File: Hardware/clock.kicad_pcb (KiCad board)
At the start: 2 copper layers, 98 x 55 mm, 53 parts, among them J1 Conn_02x05_Counter_Clockwise, J2 Conn_01x02_Male, J3 USB_B_Micro, J4 Barrel_Jack, Q1 2N7002ET1G, SW1 SW_Push, SW2 SW_Push, SW3 SW_Push, U1 STM32F103C8Tx, U2 UA78M33CDCY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

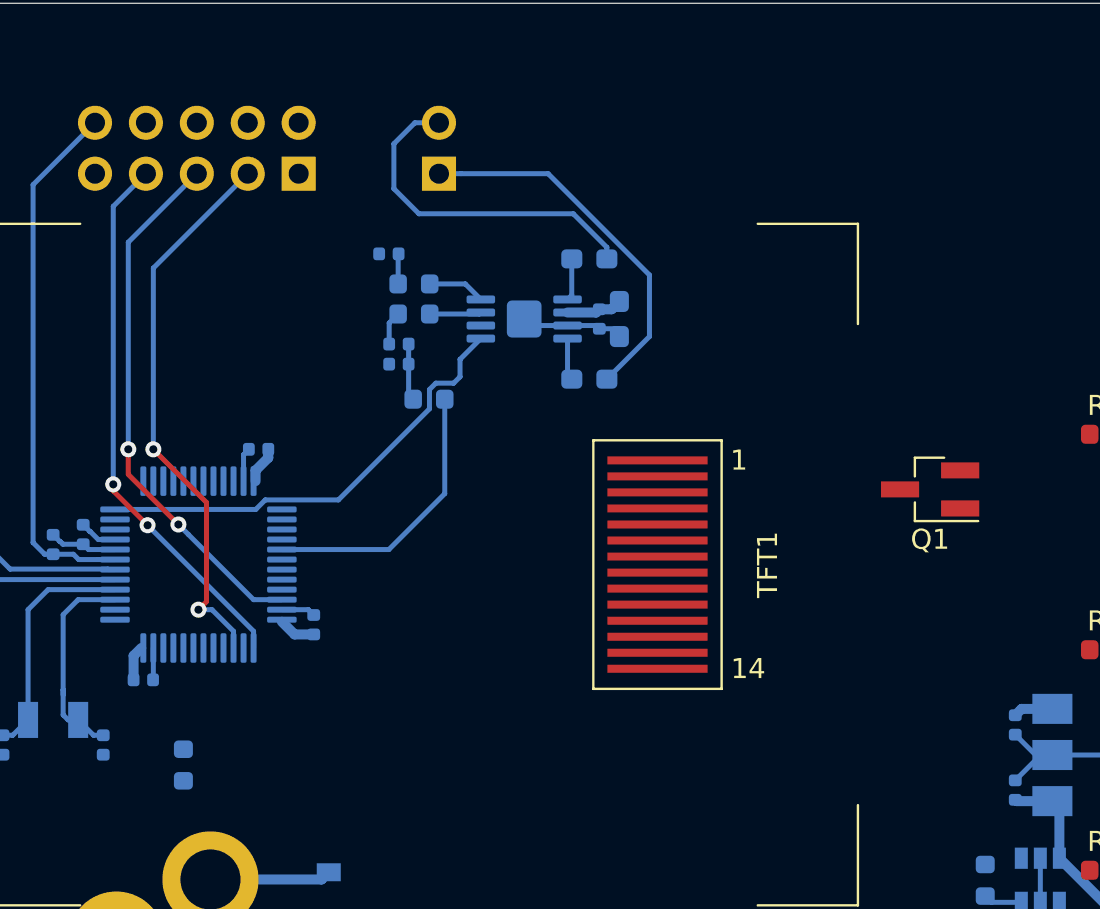
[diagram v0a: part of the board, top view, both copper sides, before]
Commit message: Added filter for amplifier supply. Some routing.
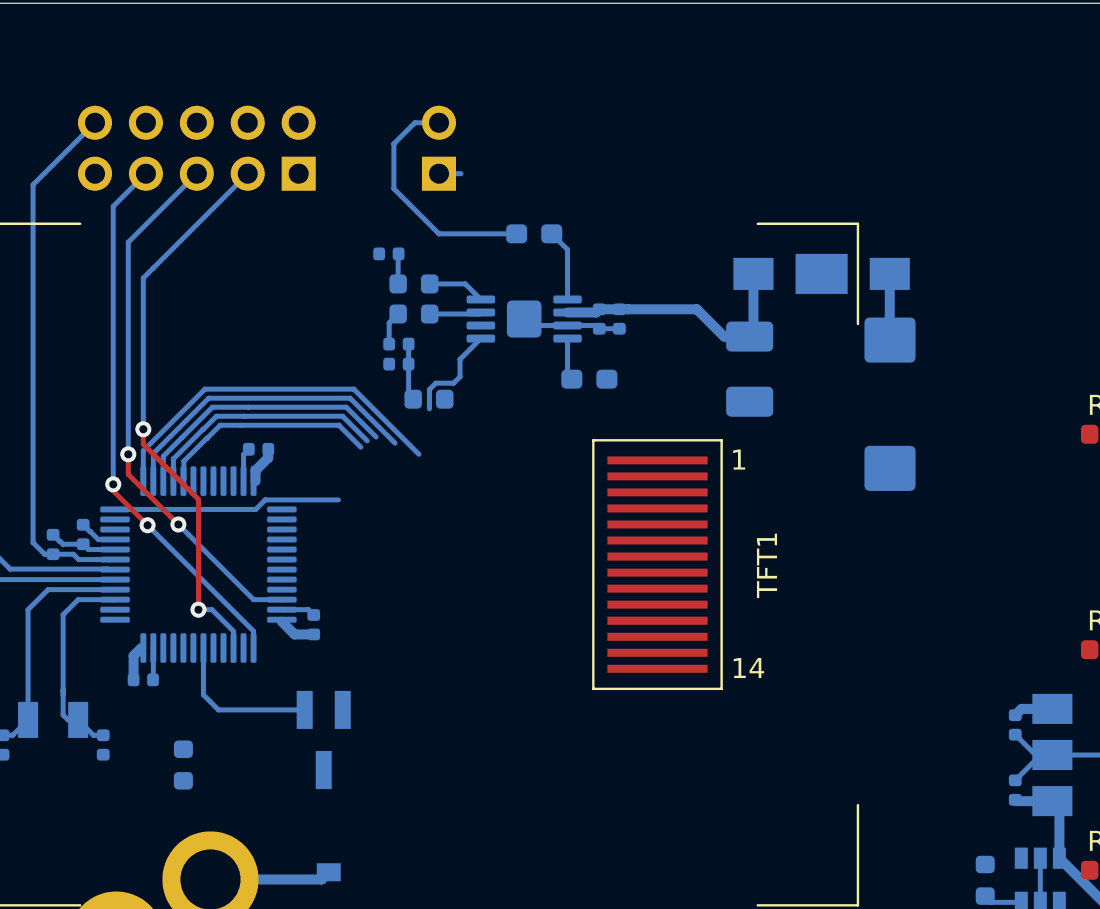
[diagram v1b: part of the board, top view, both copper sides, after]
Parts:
- added C20: 220U, Capacitor_Tantalum_SMD:CP_EIA-7343-20_Kemet-V_Pad2.25x2.55mm_HandSolder, B.Cu at (154.7, 85.7)
- added C21: 33U, Capacitor_Tantalum_SMD:CP_EIA-3528-21_Kemet-B_Pad1.50x2.35mm_HandSolder, B.Cu at (147.7, 83.9)
- added FL1: NFE61PT472C1H9L, Footprints:6816, B.Cu at (151.3, 79.2)
- C17: footprint Capacitor_SMD:C_0603_1608Metric_Pad1.05x0.95mm_HandSolder -> Capacitor_SMD:C_0402_1005Metric
- Q1: moved to B.Cu
- moved Q1 32.7 mm to (126.5, 102.4), turned to 270 degrees
- moved FB2 3.02 mm to (137.0, 77.2), turned to 0 degrees
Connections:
- C17 pad 2: +3V3 -> +3.3VA
- C18 pad 2: +3V3 -> +3.3VA
- U3 pad 6: +3V3 -> +3.3VA
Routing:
- net /TFT_RS: track 0.00 -> 17.9 mm
- net Net-(FB1-Pad1): track 18.7 -> 1.10 mm
- net /TFT_CS: track 0.00 -> 15.5 mm
- net /AUDIO: track 14.0 -> 0.00 mm
- net /TFT_SCLK: track 0.00 -> 13.5 mm
- net +3.3VA: track 0.00 -> 12.9 mm
- net /TFT_DC: track 0.00 -> 12.2 mm
- net /TFT_MOSI: track 0.00 -> 11.0 mm
- net /TFT_BL: track 0.00 -> 7.70 mm
- net /AMP_ON: track 22.9 -> 16.4 mm
- net Net-(FB2-Pad1): track 17.3 -> 12.0 mm
- net /AUDIO_OUT_+: track 2.11 -> 3.60 mm

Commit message: Routing complete
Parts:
- added R11: 100R, Resistor_SMD:R_0603_1608Metric, B.Cu at (122.2, 100.7)
- C15, C16, C19: moved to F.Cu
- J4: footprint Foodprints:PJ-102A -> Footprints:DC-005-SMT
- moved C19 126.8 mm to (155.0, 90.9), turned to 180 degrees
- moved C16 106.2 mm to (155.0, 95.7), turned to 180 degrees
- moved C15 87.1 mm to (155.0, 96.7), turned to 180 degrees
- moved D3 13.8 mm to (113.0, 109.9), turned to 270 degrees
- moved J4 11.3 mm to (122.0, 107.4), turned to 270 degrees
- moved R8 6.19 mm to (126.2, 82.5), turned to 180 degrees
- moved C12 2.56 mm to (128.2, 82.0), turned to 270 degrees
- moved R7 1.21 mm to (166.5, 87.8), turned to 90 degrees
- moved R5 1.14 mm to (166.5, 98.3), turned to 90 degrees
- moved R6 1.14 mm to (166.5, 109.3), turned to 90 degrees
- moved C5 0.56 mm to (113.9, 92.2)
- moved C13 0.51 mm to (129.7, 82.5), turned to 180 degrees
- moved C1 0.50 mm to (126.0, 96.2)
- moved C8 0.50 mm to (112.5, 92.7)
- moved TFT1 0.10 mm to (130.1, 93.7)
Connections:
- Q1 pad 1: /TFT_BL -> Net-(Q1-Pad1)
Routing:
- net +3V3: track 42.7 -> 252.4 mm, vias 0 -> 8
- net +5V: track 9.54 -> 170.7 mm
- net /BTN_DN: track 10.6 -> 101.1 mm, vias 0 -> 1
- net /BTN_UP: track 10.6 -> 93.6 mm, vias 0 -> 1
- net /SWDIO: track 26.4 -> 87.3 mm, vias 2 -> 0
- net /3VB: track 0.00 -> 56.2 mm, vias 0 -> 2
- net /SWCLK: track 27.2 -> 78.1 mm, vias 2 -> 0
- net /BTN_SEL: track 10.5 -> 60.9 mm, vias 0 -> 3
- net /SWO: track 28.1 -> 77.8 mm, vias 2 -> 0
- net /USB_DM: track 5.17 -> 47.8 mm
- net /USB_DP: track 3.87 -> 45.3 mm
- net Net-(FB1-Pad1): track 1.10 -> 34.6 mm
- net GND: track 39.2 -> 71.0 mm, vias 0 -> 32
- net /LED-: track 0.00 -> 24.4 mm, vias 0 -> 3
- net /AUDIO: track 0.00 -> 22.5 mm
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- added copper zone on B.Cu, net GND
- added copper zone on F.Cu, net GND
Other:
- board text added: "3V3"
- board text added: "CLK"
- board text added: "GND"
- board text added: "RST"
- board text added: "SPEAKER"
- board text added: "SWD"
- board text added: "SWO"
- board text removed: "Barrel jack PTH over TFT area, may need to move"

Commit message: DC jack was round the wrong way. Added proper step model for it. Added Freecad model.
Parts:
- moved J4 15.4 mm to (122.1, 122.8), turned to 90 degrees
- moved J2 8.00 mm to (140.2, 74.2)
- moved J1 7.03 mm to (132.2, 73.5)
- moved FB2 1.93 mm to (138.6, 78.2), turned to 270 degrees
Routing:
- net Net-(D3-Pad2): track 9.54 -> 24.3 mm
- net /RESET: track 44.8 -> 58.6 mm
- net Net-(FB1-Pad1): track 34.6 -> 26.6 mm
- net /SWCLK: track 78.1 -> 86.0 mm
- net /SWDIO: track 87.3 -> 94.4 mm
- net /SWO: track 77.8 -> 84.8 mm
- net Net-(FB2-Pad1): track 9.97 -> 6.36 mm
- net +3V3: track 252.4 -> 249.8 mm, vias 8 -> 9
- net /AUDIO_OUT_+: track 3.60 -> 1.39 mm
- net +5V: track 170.7 -> 168.8 mm
- net /BTN_UP: track 93.6 -> 92.3 mm
- net /BTN_DN: track 101.1 -> 99.8 mm
- net GND: vias 32 -> 31
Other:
- board text removed: "3V3"
- board text removed: "CLK"
- board text removed: "GND"
- board text removed: "RST"
- board text removed: "SWD"
- board text removed: "SWO"

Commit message: Added FreeCAD model of enclosure + PCB. Small changes to PCB layout. Added STEP model of TFT display.
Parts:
- U3: footprint Package_SO:MSOP-8-1EP_3x3mm_P0.65mm_EP1.73x1.85mm -> Package_SO:MSOP-8-1EP_3x3mm_P0.65mm_EP1.73x1.85mm_ThermalVias
- moved FB2 0.23 mm to (138.6, 78.0)
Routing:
- net GND: track 71.0 -> 74.7 mm, vias 31 -> 32
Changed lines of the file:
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@@
     (thickness 1.6)
     (drawings 8797)
-    (tracks 577)
+    (tracks 580)
     (zones 0)
     (modules 57)
@@
   (page A4)
   (layers
-    (0 F.Cu signal)
+    (0 F.Cu signal hide)
     (31 B.Cu signal)
     (34 B.Paste user hide)
@@
     (44 Edge.Cuts user)
     (45 Margin user)
-    (46 B.CrtYd user hide)
-    (47 F.CrtYd user)
+    (46 B.CrtYd user)
+    (47 F.CrtYd user hide)
   )
   (setup
-    (last_trace_width 1)
+    (last_trace_width 0.25)
     (user_trace_width 0.24)
     (user_trace_width 0.5)
@@
     (uvia_drill 0.1)
   )
+  (module Package_SO:MSOP-8-1EP_3x3mm_P0.65mm_EP1.73x1.85mm_ThermalVias (layer B.Cu)
+    (at 136.4639 81.4)
+    (descr "MSOP, 8 Pin (http://www.ti.com/lit/ds/symlink/lm25085.pdf#page=32), generated with kicad-footprint-generator ipc_gullwing_generator.py")
+    (tags "MSOP SO")
+    (attr smd)
+    (fp_text reference U3 (at 0 2.45) (layer B.SilkS)
+      (effects (font (size 1 1) (thickness 0.15)) (justify mirror))
+    )
+    (fp_text value TPA2005D1DRB (at 0 -2.45) (layer B.Fab)
+      (effects (font (size 1 1) (thickness 0.15)) (justify mirror))
+    )
+    (fp_text user %R (at 0 0) (layer B.Fab)
+      (effects (font (size 0.75 0.75) (thickness 0.11)) (justify mirror))
+    )
+    (fp_line (start 3.12 1.75) (end -3.12 1.75) (layer B.CrtYd) (width 0.05))
+    (fp_line (start 3.12 -1.75) (end 3.12 1.75) (layer B.CrtYd) (width 0.05))
+    (fp_line (start -3.12 -1.75) (end 3.12 -1.75) (layer B.CrtYd) (width 0.05))
+    (fp_line (start -3.12 1.75) (end -3.12 -1.75) (layer B.CrtYd) (width 0.05))
+    (fp_line (start -1.5 0.75) (end -0.75 1.5) (layer B.Fab) (width 0.1))
+    (fp_line (start -1.5 -1.5) (end -1.5 0.75) (layer B.Fab) (width 0.1))
+    (fp_line (start 1.5 -1.5) (end -1.5 -1.5) (layer B.Fab) (width 0.1))
+    (fp_line (start 1.5 1.5) (end 1.5 -1.5) (layer B.Fab) (width 0.1))
+    (fp_line (start -0.75 1.5) (end 1.5 1.5) (layer B.Fab) (width 0.1))
+    (fp_line (start 0 1.61) (end -2.875 1.61) (layer B.SilkS) (width 0.12))
+    (fp_line (start 0 1.61) (end 1.5 1.61) (layer B.SilkS) (width 0.12))
+    (fp_line (start 0 -1.61) (end -1.5 -1.61) (layer B.SilkS) (width 0.12))
+    (fp_line (start 0 -1.61) (end 1.5 -1.61) (layer B.SilkS) (width 0.12))
+    (pad 8 smd roundrect (at 2.1625 0.975) (size 1.425 0.4) (layers B.Cu B.Paste B.Mask) (roundrect_rratio 0.25)
+      (net 19 /AUDIO_OUT_-))
+    (pad 7 smd roundrect (at 2.1625 0.325) (size 1.425 0.4) (layers B.Cu B.Paste B.Mask) (roundrect_rratio 0.25)
+      (net 2 GND))
+    (pad 6 smd roundrect (at 2.1625 -0.325) (size 1.425 0.4) (layers B.Cu B.Paste B.Mask) (roundrect_rratio 0.25)
+      (net 65 +3.3VA))
+    (pad 5 smd roundrect (at 2.1625 -0.975) (size 1.425 0.4) (layers B.Cu B.Paste B.Mask) (roundrect_rratio 0.25)
+      (net 20 /AUDIO_OUT_+))
+    (pad 4 smd roundrect (at -2.1625 -0.975) (size 1.425 0.4) (layers B.Cu B.Paste B.Mask) (roundrect_rratio 0.25)
+      (net 39 "Net-(R10-Pad1)"))
+    (pad 3 smd roundrect (at -2.1625 -0.325) (size 1.425 0.4) (layers B.Cu B.Paste B.Mask) (roundrect_rratio 0.25)
+      (net 38 "Net-(R9-Pad1)"))
+    (pad 2 smd roundrect (at -2.1625 0.325) (size 1.425 0.4) (layers B.Cu B.Paste B.Mask) (roundrect_rratio 0.25))
+    (pad 1 smd roundrect (at -2.1625 0.975) (size 1.425 0.4) (layers B.Cu B.Paste B.Mask) (roundrect_rratio 0.25)
+      (net 48 /AMP_ON))
+    (pad "" smd roundrect (at 0.43 -0.46) (size 0.72 0.77) (layers B.Paste) (roundrect_rratio 0.25))
+    (pad "" smd roundrect (at 0.43 0.46) (size 0.72 0.77) (layers B.Paste) (roundrect_rratio 0.25))
+    (pad "" smd roundrect (at -0.43 -0.46) (size 0.72 0.77) (layers B.Paste) (roundrect_rratio 0.25))
+    (pad "" smd roundrect (at -0.43 0.46) (size 0.72 0.77) (layers B.Paste) (roundrect_rratio 0.25))
+    (pad 9 smd roundrect (at 0 0) (size 1.6 1.8) (layers F.Cu) (roundrect_rratio 0.15625)
+      (net 2 GND))
+    (pad 9 thru_hole circle (at 0.55 -0.65) (size 0.5 0.5) (drill 0.2) (layers *.Cu)
+      (net 2 GND))
+    (pad 9 thru_hole circle (at -0.55 -0.65) (size 0.5 0.5) (drill 0.2) (layers *.Cu)
+      (net 2 GND))
+    (pad 9 thru_hole circle (at 0.55 0.65) (size 0.5 0.5) (drill 0.2) (layers *.Cu)
+      (net 2 GND))
+    (pad 9 thru_hole circle (at -0.55 0.65) (size 0.5 0.5) (drill 0.2) (layers *.Cu)
+      (net 2 GND))
+    (pad 9 smd roundrect (at 0 0) (size 1.73 1.85) (layers B.Cu B.Mask) (roundrect_rratio 0.144509)
+      (net 2 GND))
+    (model ${KISYS3DMOD}/Package_SO.3dshapes/MSOP-8-1EP_3x3mm_P0.65mm_EP1.73x1.85mm.wrl
+      (at (xyz 0 0 0))
+      (scale (xyz 1 1 1))
+      (rotate (xyz 0 0 0))
+    )
+  )
   (module Footprints:DC-005-SMT (layer B.Cu)
     (at 122.1479 122.8165 90)
@@
   )
   (module Resistor_SMD:R_0603_1608Metric_Pad1.05x0.95mm_HandSolder (layer B.Cu)
-    (at 138.5944 78.176 270)
+    (at 138.5944 77.95 270)
     (descr "Resistor SMD 0603 (1608 Metric), square (rectangular) end terminal, IPC_7351 nominal with elongated pad for handsoldering. (Body size source: http://www.tortai-tech.com/upload/download/2011102023233369053.pdf), generated with kicad-footprint-generator")
     (tags "resistor handsolder")
@@
     )
   )
-  (module Package_SO:MSOP-8-1EP_3x3mm_P0.65mm_EP1.73x1.85mm (layer B.Cu)
-    (at 136.4639 81.4)
-    (descr "MSOP, 8 Pin (http://www.ti.com/lit/ds/symlink/lm25085.pdf#page=32), generated with kicad-footprint-generator ipc_gullwing_generator.py")
-    (tags "MSOP SO")
-    (attr smd)
-    (fp_text reference U3 (at 0 2.45) (layer B.SilkS)
-      (effects (font (size 1 1) (thickness 0.15)) (justify mirror))
-    )
-    (fp_text value TPA2005D1DRB (at 0 -2.45) (layer B.Fab)
-      (effects (font (size 1 1) (thickness 0.15)) (justify mirror))
-    )
-    (fp_line (start 0 -1.61) (end 1.5 -1.61) (layer B.SilkS) (width 0.12))
-    (fp_line (start 0 -1.61) (end -1.5 -1.61) (layer B.SilkS) (width 0.12))
-    (fp_line (start 0 1.61) (end 1.5 1.61) (layer B.SilkS) (width 0.12))
-    (fp_line (start 0 1.61) (end -2.875 1.61) (layer B.SilkS) (width 0.12))
-    (fp_line (start -0.75 1.5) (end 1.5 1.5) (layer B.Fab) (width 0.1))
-    (fp_line (start 1.5 1.5) (end 1.5 -1.5) (layer B.Fab) (width 0.1))
-    (fp_line (start 1.5 -1.5) (end -1.5 -1.5) (layer B.Fab) (width 0.1))
-    (fp_line (start -1.5 -1.5) (end -1.5 0.75) (layer B.Fab) (width 0.1))
-    (fp_line (start -1.5 0.75) (end -0.75 1.5) (layer B.Fab) (width 0.1))
-    (fp_line (start -3.12 1.75) (end -3.12 -1.75) (layer B.CrtYd) (width 0.05))
-    (fp_line (start -3.12 -1.75) (end 3.12 -1.75) (layer B.CrtYd) (width 0.05))
-    (fp_line (start 3.12 -1.75) (end 3.12 1.75) (layer B.CrtYd) (width 0.05))
-    (fp_line (start 3.12 1.75) (end -3.12 1.75) (layer B.CrtYd) (width 0.05))
-    (fp_text user %R (at 0 0) (layer B.Fab)
-      (effects (font (size 0.75 0.75) (thickness 0.11)) (justify mirror))
-    )
-    (pad 9 smd roundrect (at 0 0) (size 1.73 1.85) (layers B.Cu B.Mask) (roundrect_rratio 0.144509)
-      (net 2 GND))
-    (pad "" smd roundrect (at -0.43 0.46) (size 0.7 0.75) (layers B.Paste) (roundrect_rratio 0.25))
-    (pad "" smd roundrect (at -0.43 -0.46) (size 0.7 0.75) (layers B.Paste) (roundrect_rratio 0.25))
-    (pad "" smd roundrect (at 0.43 0.46) (size 0.7 0.75) (layers B.Paste) (roundrect_rratio 0.25))
-    (pad "" smd roundrect (at 0.43 -0.46) (size 0.7 0.75) (layers B.Paste) (roundrect_rratio 0.25))
-    (pad 1 smd roundrect (at -2.1625 0.975) (size 1.425 0.4) (layers B.Cu B.Paste B.Mask) (roundrect_rratio 0.25)
-      (net 48 /AMP_ON))
-    (pad 2 smd roundrect (at -2.1625 0.325) (size 1.425 0.4) (layers B.Cu B.Paste B.Mask) (roundrect_rratio 0.25))
-    (pad 3 smd roundrect (at -2.1625 -0.325) (size 1.425 0.4) (layers B.Cu B.Paste B.Mask) (roundrect_rratio 0.25)
-      (net 38 "Net-(R9-Pad1)"))
-    (pad 4 smd roundrect (at -2.1625 -0.975) (size 1.425 0.4) (layers B.Cu B.Paste B.Mask) (roundrect_rratio 0.25)
-      (net 39 "Net-(R10-Pad1)"))
-    (pad 5 smd roundrect (at 2.1625 -0.975) (size 1.425 0.4) (layers B.Cu B.Paste B.Mask) (roundrect_rratio 0.25)
-      (net 20 /AUDIO_OUT_+))
-    (pad 6 smd roundrect (at 2.1625 -0.325) (size 1.425 0.4) (layers B.Cu B.Paste B.Mask) (roundrect_rratio 0.25)
-      (net 65 +3.3VA))
-    (pad 7 smd roundrect (at 2.1625 0.325) (size 1.425 0.4) (layers B.Cu B.Paste B.Mask) (roundrect_rratio 0.25)
-      (net 2 GND))
-    (pad 8 smd roundrect (at 2.1625 0.975) (size 1.425 0.4) (layers B.Cu B.Paste B.Mask) (roundrect_rratio 0.25)
-      (net 19 /AUDIO_OUT_-))
-    (model ${KISYS3DMOD}/Package_SO.3dshapes/MSOP-8-1EP_3x3mm_P0.65mm_EP1.73x1.85mm.wrl
-      (at (xyz 0 0 0))
-      (scale (xyz 1 1 1))
-      (rotate (xyz 0 0 0))
-    )
-    (model ${KIPRJMOD}/3D/MSOP-8.step
-      (at (xyz 0 0 0))
-      (scale (xyz 1 1 1))
-      (rotate (xyz -90 0 90))
-    )
-  )
   (module Crystal:Crystal_HC49-U_Vertical (layer B.Cu)
     (at 107.9639 95.9 90)
@@
     (pad 14 smd rect (at 12.9 5.2) (size 5 0.4) (layers F.Cu F.Paste F.Mask)
       (net 46 "Net-(TFT1-Pad14)"))
+    (model ${KIPRJMOD}/3D/SPE_IM120905001_FPC.stp
+      (offset (xyz -21 -17 0.2))
+      (scale (xyz 1 1 1))
+      (rotate (xyz 0 0 0))
+    )
   )
   (gr_text SPEAKER (at 153.8979 72.7785) (layer B.SilkS)
@@
   (via (at 105.2569 67.5715) (size 1.2) (drill 0.8) (layers F.Cu B.Cu) (net 2))
   (via (at 114.0199 80.9065) (size 0.8) (drill 0.4) (layers F.Cu B.Cu) (net 2))
+  (via (at 135.9139 77.95) (size 1.2) (drill 0.8) (layers F.Cu B.Cu) (net 2))
+  (segment (start 135.9139 80.85) (end 136.4639 81.4) (width 0.25) (layer F.Cu) (net 2))
+  (segment (start 135.9139 77.95) (end 135.9139 80.85) (width 0.25) (layer F.Cu) (net 2))
   (via (at 125.3139 97.45) (size 0.8) (drill 0.4) (layers F.Cu B.Cu) (net 3))
   (via (at 171.4139 78.85) (size 1.2) (drill 0.8) (layers F.Cu B.Cu) (net 3))

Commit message: Added weka to silkscreen.
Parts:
- added G***: LOGO, Footprints:weka, B.Cu at (176.9, 93.5)
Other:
- board text added: "JLCJLCJLCJLC"
- board text added: "STM32F103 Powered Alarm Clock"
